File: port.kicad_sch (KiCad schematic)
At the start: 15 parts, among them J12 Conn_02x03, U9 FIN1019M

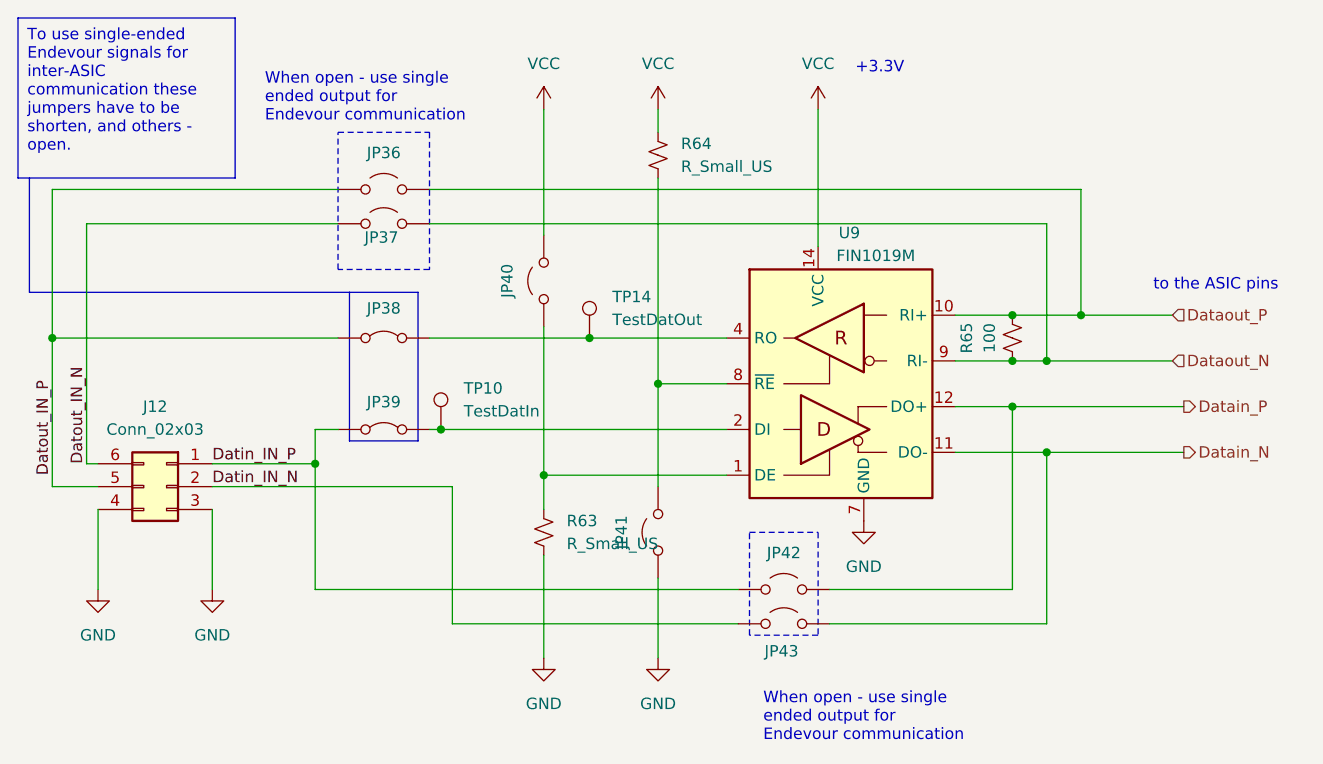
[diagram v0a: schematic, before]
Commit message: add mounting holes, make the board and the zones of rectangular shape, add sikscreen text
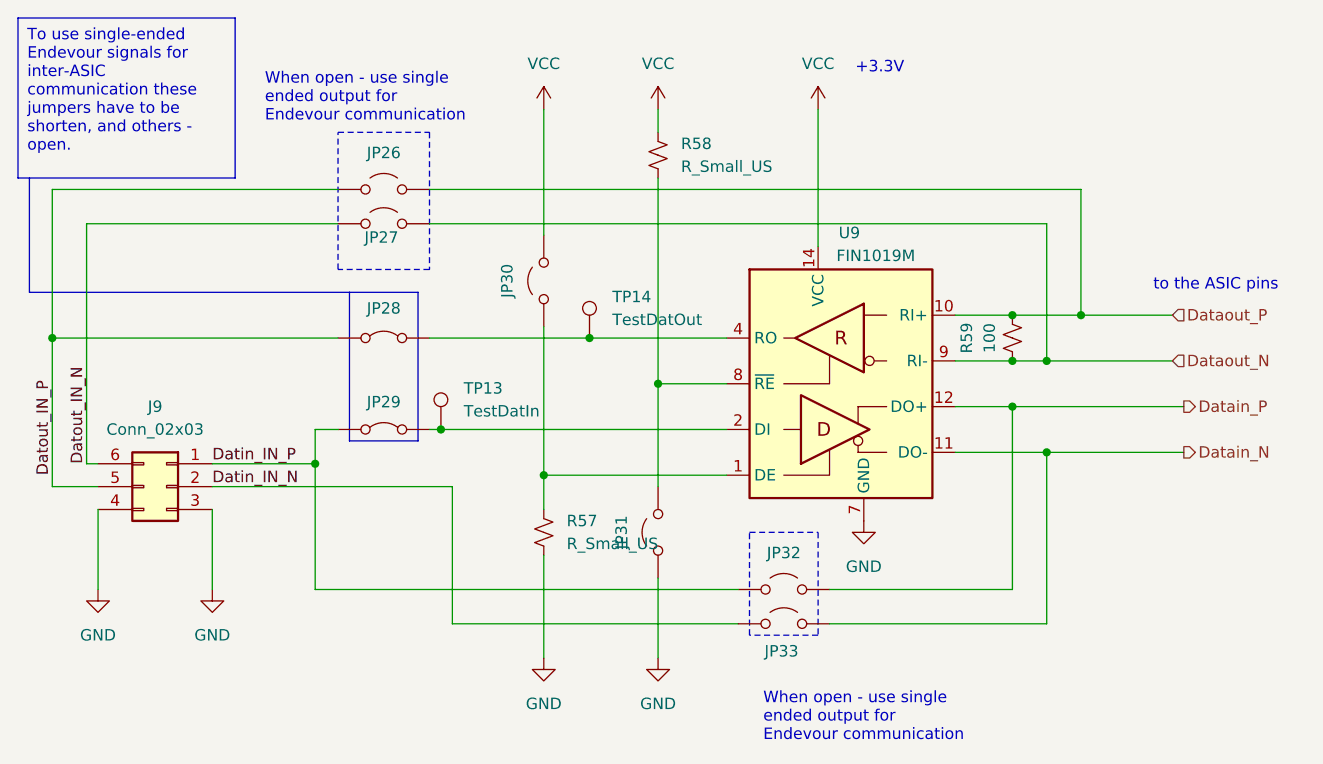
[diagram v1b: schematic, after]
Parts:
- renumbered J12 to J9, JP36 to JP26, JP37 to JP27, JP38 to JP28, JP39 to JP29, JP40 to JP30, JP41 to JP31, JP42 to JP32, JP43 to JP33, R63 to R57, R64 to R58, R65 to R59, TP10 to TP13
